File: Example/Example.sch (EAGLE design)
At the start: 13 parts, among them IC1 LM555D, J1 UX60-MB-5S8, Q1 SSM3J356R, Q2 BSS806N, SW1 MFS101D-6-Z

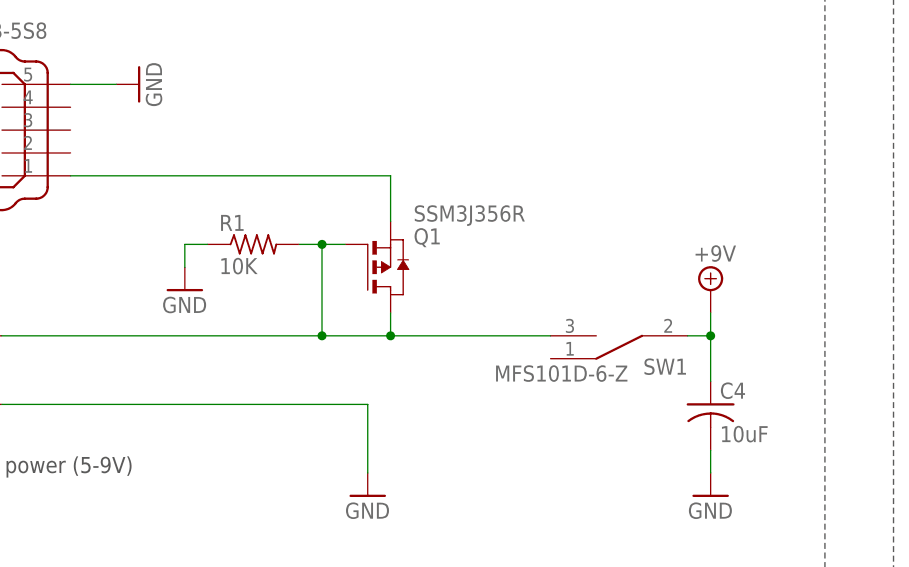
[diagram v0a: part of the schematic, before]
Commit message: Fixed broken circuit and made new render
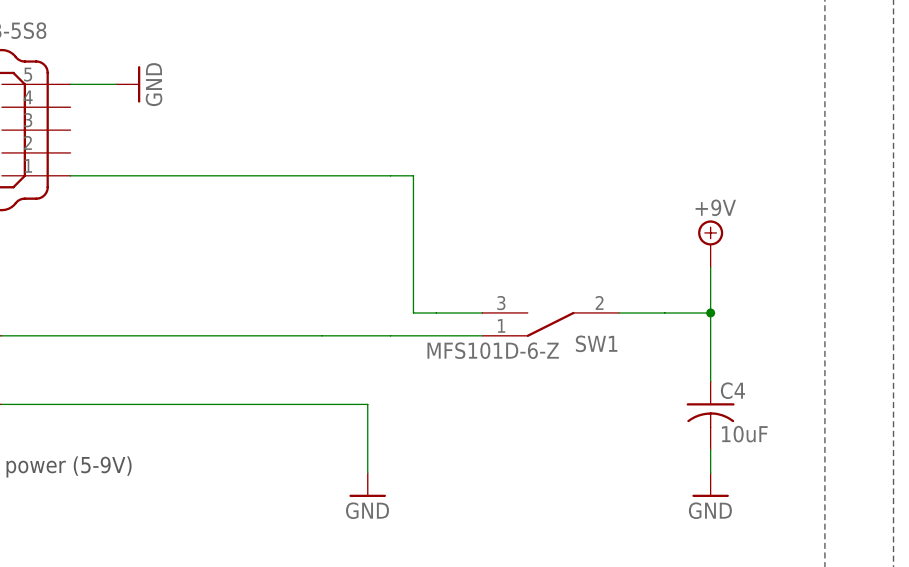
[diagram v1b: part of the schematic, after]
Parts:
- removed Q1: SSM3J356R, Example:SSM3J356R
- removed R1: 10K, rcl:R-US_R0603
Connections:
- net GND: no longer R1.1
- net N$4: now also SW1.B; no longer Q1.S
- net N$6: now also SW1.A; no longer Q1.D, Q1.G, R1.2, SW1.B
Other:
- moved on the sheet: SW1
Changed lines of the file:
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@@
 <?xml version="1.0" encoding="utf-8"?>
 <!DOCTYPE eagle SYSTEM "eagle.dtd">
-<eagle version="9.6.2">
+<eagle version="9.5.2">
 <drawing>
 <settings>
@@
 <part name="SUPPLY12" library="RoboJackets-Supplies" deviceset="GND" device=""/>
 <part name="SW1" library="Example" deviceset="MFS101D-6-Z" device="" override_package3d_urn="urn:adsk.eagle:package:25000897/2" override_package_urn="urn:adsk.eagle:footprint:25000899/1"/>
-<part name="SUPPLY13" library="RoboJackets-Supplies" deviceset="GND" device=""/>
-<part name="R1" library="rcl" library_urn="urn:adsk.eagle:library:334" deviceset="R-US_" device="R0603" package3d_urn="urn:adsk.eagle:package:23555/3" value="10K"/>
-<part name="Q1" library="Example" deviceset="SSM3J356R" device="" package3d_urn="urn:adsk.eagle:package:24993154/1"/>
 </parts>
 <sheets>
@@
 <attribute name="VALUE" x="83.82" y="134.62" size="1.778" layer="96"/>
 </instance>
-<instance part="SUPPLY9" gate="+9V" x="124.46" y="160.02" smashed="yes">
-<attribute name="VALUE" x="122.555" y="163.195" size="1.778" layer="96"/>
+<instance part="SUPPLY9" gate="+9V" x="124.46" y="165.1" smashed="yes">
+<attribute name="VALUE" x="122.555" y="168.275" size="1.778" layer="96"/>
 </instance>
 <instance part="SUPPLY10" gate="G$1" x="27.94" y="55.88" smashed="yes">
@@
 <attribute name="VALUE" x="121.92" y="134.62" size="1.778" layer="96"/>
 </instance>
-<instance part="SW1" gate="G$1" x="114.3" y="154.94" smashed="yes" rot="R180">
-<attribute name="NAME" x="121.92" y="152.4" size="1.778" layer="95" rot="R180"/>
-<attribute name="VALUE" x="115.316" y="151.638" size="1.778" layer="96" rot="R180"/>
-</instance>
-<instance part="SUPPLY13" gate="G$1" x="66.04" y="160.02" smashed="yes">
-<attribute name="VALUE" x="63.5" y="157.48" size="1.778" layer="96"/>
-</instance>
-<instance part="R1" gate="G$1" x="73.66" y="165.1" smashed="yes">
-<attribute name="NAME" x="69.85" y="166.5986" size="1.778" layer="95"/>
-<attribute name="VALUE" x="69.85" y="161.798" size="1.778" layer="96"/>
-</instance>
-<instance part="Q1" gate="G$1" x="88.9" y="162.56" smashed="yes">
-<attribute name="VALUE" x="91.44" y="167.64" size="1.778" layer="96"/>
-<attribute name="NAME" x="91.44" y="165.1" size="1.778" layer="95"/>
+<instance part="SW1" gate="G$1" x="106.68" y="157.48" smashed="yes" rot="R180">
+<attribute name="NAME" x="114.3" y="154.94" size="1.778" layer="95" rot="R180"/>
+<attribute name="VALUE" x="107.696" y="154.178" size="1.778" layer="96" rot="R180"/>
 </instance>
 </instances>
@@
 <pinref part="C4" gate="G$1" pin="2"/>
 <wire x1="124.46" y1="139.7" x2="124.46" y2="142.24" width="0.1524" layer="91"/>
-</segment>
-<segment>
-<pinref part="SUPPLY13" gate="G$1" pin="GND"/>
-<wire x1="66.04" y1="162.56" x2="66.04" y2="165.1" width="0.1524" layer="91"/>
-<pinref part="R1" gate="G$1" pin="1"/>
-<wire x1="66.04" y1="165.1" x2="68.58" y2="165.1" width="0.1524" layer="91"/>
 </segment>
 </net>
@@
 <segment>
 <pinref part="SUPPLY9" gate="+9V" pin="+9V"/>
-<wire x1="124.46" y1="154.94" x2="124.46" y2="157.48" width="0.1524" layer="91"/>
-<wire x1="121.92" y1="154.94" x2="124.46" y2="154.94" width="0.1524" layer="91"/>
+<wire x1="124.46" y1="157.48" x2="124.46" y2="162.56" width="0.1524" layer="91"/>
+<wire x1="114.3" y1="157.48" x2="119.38" y2="157.48" width="0.1524" layer="91"/>
+<wire x1="119.38" y1="157.48" x2="124.46" y2="157.48" width="0.1524" layer="91"/>
 <pinref part="C4" gate="G$1" pin="1"/>
-<wire x1="124.46" y1="149.86" x2="124.46" y2="154.94" width="0.1524" layer="91"/>
-<junction x="124.46" y="154.94"/>
+<wire x1="124.46" y1="149.86" x2="124.46" y2="157.48" width="0.1524" layer="91"/>
+<junction x="124.46" y="157.48"/>
 <pinref part="SW1" gate="G$1" pin="COMMON"/>
 </segment>
@@
 <pinref part="J1" gate="G$1" pin="1"/>
 <wire x1="53.34" y1="172.72" x2="88.9" y2="172.72" width="0.1524" layer="91"/>
-<wire x1="88.9" y1="172.72" x2="88.9" y2="167.64" width="0.1524" layer="91"/>
-<pinref part="Q1" gate="G$1" pin="S"/>
+<wire x1="88.9" y1="172.72" x2="91.44" y2="172.72" width="0.1524" layer="91"/>
+<wire x1="91.44" y1="172.72" x2="91.44" y2="157.48" width="0.1524" layer="91"/>
+<wire x1="91.44" y1="157.48" x2="93.98" y2="157.48" width="0.1524" layer="91"/>
+<pinref part="SW1" gate="G$1" pin="B"/>
+<wire x1="93.98" y1="157.48" x2="99.06" y2="157.48" width="0.1524" layer="91"/>
 </segment>
 </net>
 <net name="N$6" class="0">
 <segment>
-<pinref part="R1" gate="G$1" pin="2"/>
-<wire x1="83.82" y1="165.1" x2="81.28" y2="165.1" width="0.1524" layer="91"/>
-<pinref part="Q1" gate="G$1" pin="G"/>
 <pinref part="J2" gate="G$1" pin="1"/>
-<wire x1="81.28" y1="165.1" x2="78.74" y2="165.1" width="0.1524" layer="91"/>
 <wire x1="45.72" y1="154.94" x2="81.28" y2="154.94" width="0.1524" layer="91"/>
-<pinref part="SW1" gate="G$1" pin="B"/>
 <wire x1="81.28" y1="154.94" x2="88.9" y2="154.94" width="0.1524" layer="91"/>
-<wire x1="88.9" y1="154.94" x2="106.68" y2="154.94" width="0.1524" layer="91"/>
-<wire x1="88.9" y1="157.48" x2="88.9" y2="154.94" width="0.1524" layer="91"/>
-<junction x="88.9" y="154.94"/>
-<pinref part="Q1" gate="G$1" pin="D"/>
-<wire x1="81.28" y1="165.1" x2="81.28" y2="154.94" width="0.1524" layer="91"/>
-<junction x="81.28" y="165.1"/>
-<junction x="81.28" y="154.94"/>
-</segment>
-</net>
+<pinref part="SW1" gate="G$1" pin="A"/>
+<wire x1="99.06" y1="154.94" x2="88.9" y2="154.94" width="0.1524" layer="91"/>
+</segment>
+</net>
